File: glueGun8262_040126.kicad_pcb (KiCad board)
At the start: 2 copper layers, 121.9 x 76.8 mm, 62 parts, among them CN1 KF243-5.0-2P, CN2 KF243-5.0-2P, CN3 KF243-5.0-2P, CN4 KF243-5.0-2P, CN5 KF243-5.0-2P, CN6 KF243-5.0-2P, CN7 KF243-5.0-2P, CN9 KF243-5.0-4P, U1 DRV8262DDWR, U10 INA240A2DR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

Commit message: no drcErrors2 before replacing U5 to smt
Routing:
- net +48V: track 298.8 -> 284.9 mm
- net Net-(CN9-Pad4): track 11.4 -> 13.9 mm
- net Net-(U11-IN-): track 22.0 -> 19.7 mm
- net Net-(D4-K): track 7.27 -> 8.82 mm
- net /U1_OUT2: track 28.8 -> 29.5 mm
- net /U1_OUT3: track 14.9 -> 15.7 mm
- net Net-(D5-K): track 9.85 -> 10.6 mm
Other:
- board size 121.9 x 76.8 mm -> 121.9 x 78.1 mm

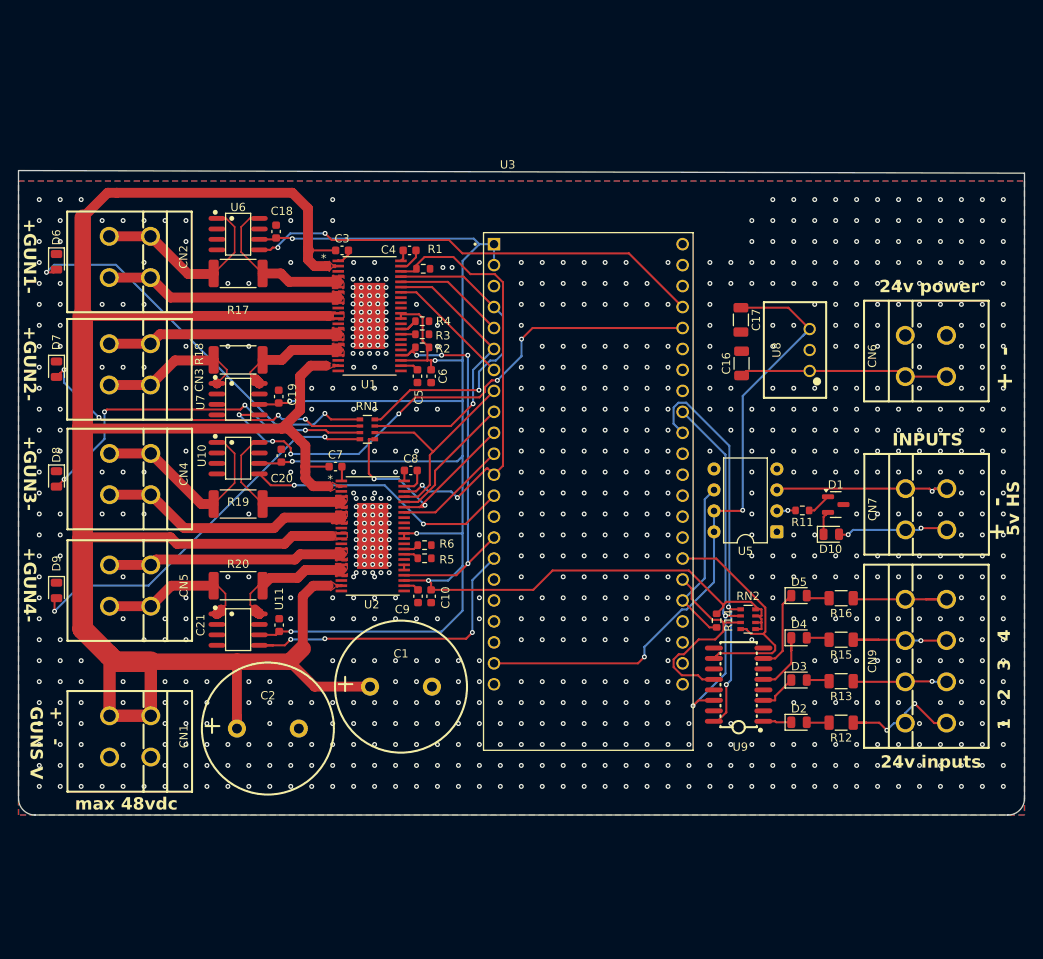
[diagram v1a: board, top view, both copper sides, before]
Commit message: added mounting holes
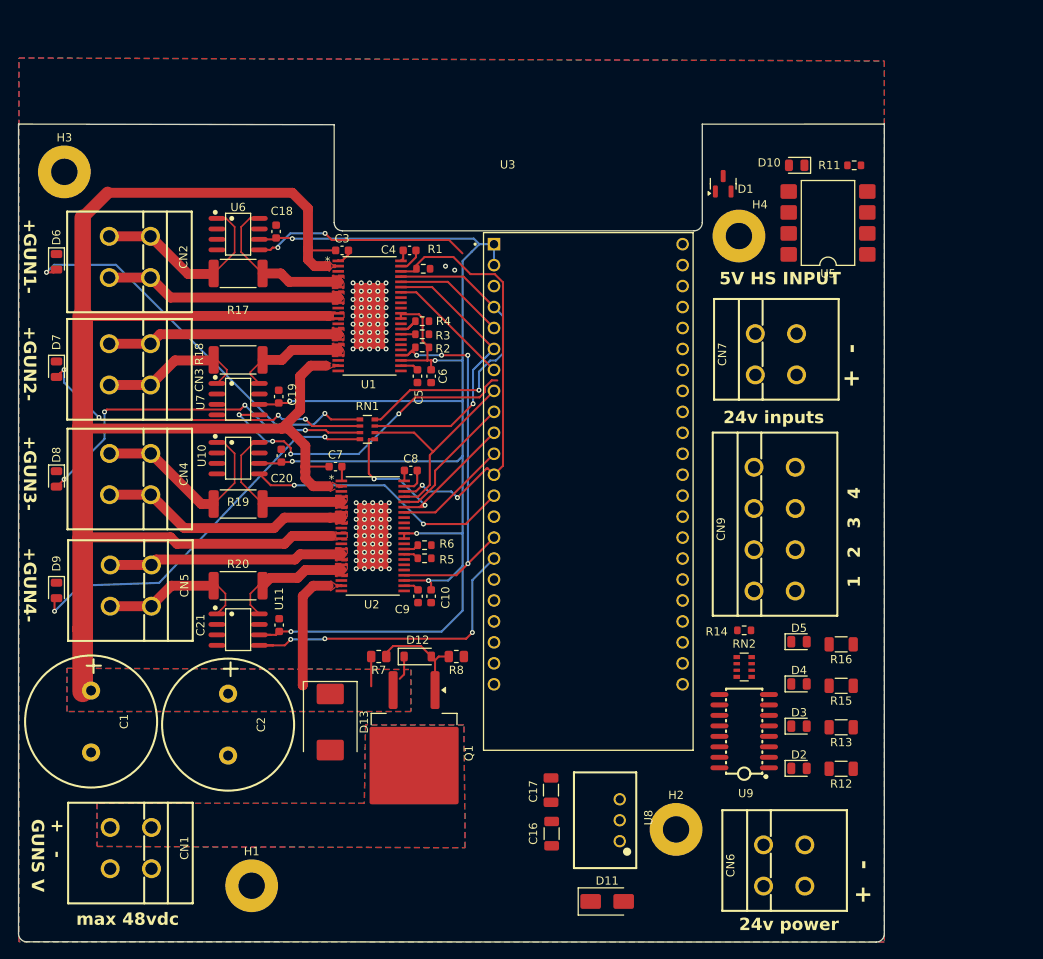
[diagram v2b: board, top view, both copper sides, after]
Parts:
- added D11: D, Diode_SMD:D_SMA, F.Cu at (177.5, 138.1)
- added D12: BZT52C15 zener, Diode_SMD:D_SOD-123, F.Cu at (154.6, 108.4)
- added D13: SMCJ51A, Diode_SMD:D_SMC, F.Cu at (144.0, 116.4)
- added H1: MountingHole_Pad, MountingHole:MountingHole_3.2mm_M3_Pad, F.Cu at (134.5, 136.2)
- added H2: MountingHole_Pad, MountingHole:MountingHole_3.2mm_M3_Pad, F.Cu at (185.9, 129.4)
- added H3: MountingHole_Pad, MountingHole:MountingHole_3.2mm_M3_Pad, F.Cu at (111.8, 49.7)
- added H4: MountingHole_Pad, MountingHole:MountingHole_3.2mm_M3_Pad, F.Cu at (193.5, 57.5)
- added Q1: SQM120P10-10m1L, Package_TO_SOT_SMD:TO-263-2, F.Cu at (154.1, 120.1)
- added R7: 100k, Resistor_SMD:R_0805_2012Metric, F.Cu at (149.9, 108.4)
- added R8: 47k, Resistor_SMD:R_0805_2012Metric, F.Cu at (159.3, 108.4)
- C17: value 22uf 10v -> 22uf 16v
- D1: value D_Schottky -> D_Schottky_AKK
- U5: footprint Package_DIP:DIP-8_W7.62mm -> Package_DIP:SMDIP-8_W9.53mm
- moved CN6 64.1 mm to (199.0, 133.8)
- moved U8 61.5 mm to (179.1, 128.3)
- moved C16 61.5 mm to (170.8, 129.9)
- moved C17 61.5 mm to (170.7, 124.6)
- moved D10 44.9 mm to (200.5, 48.9), turned to 180 degrees
- moved R11 42.3 mm to (207.5, 48.9), turned to 0 degrees
- moved D1 41.2 mm to (191.6, 51.1), turned to 90 degrees
- moved U5 37.9 mm to (204.3, 55.9)
- moved C1 37.8 mm to (115.0, 116.3), turned to -90 degrees
- moved CN7 26.2 mm to (198.0, 71.8)
- moved CN9 24.3 mm to (197.8, 93.0)
- moved CN1 13.5 mm to (119.8, 131.6)
- moved RN2 5.81 mm to (194.2, 109.7)
- moved U9 5.67 mm to (194.2, 117.5)
- moved D2 5.59 mm to (200.8, 122.0)
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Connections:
- C16 pad 1: Net-(U8-VIN) -> Net-(D11-K)
- CN1 pad 1: +48V -> Net-(Q1-D)
- CN6 pad 1: Net-(U8-VIN) -> Net-(D11-A)
- D1 pad 1: Net-(D1-K) -> Net-(D1-A)
- D1 pad 2: Net-(D1-A) -> unconnected-(D1-K-Pad2)
- D1 pad 3: (no net) -> Net-(D1-K-Pad3)
- R11 pad 1: Net-(D1-K) -> Net-(D1-K-Pad3)
- U8 pad 1: Net-(U8-VIN) -> Net-(D11-K)
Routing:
- net +5V: track 79.5 -> 0.00 mm, vias 2 -> 0
- net +48V: track 284.9 -> 230.4 mm
- net /Input_1_24v: track 48.9 -> 0.00 mm, vias 2 -> 0
- net +3V3: track 237.1 -> 188.7 mm
- net /Input_2_24v: track 44.3 -> 0.00 mm, vias 2 -> 0
- net /Input_4_24v: track 29.6 -> 0.00 mm
- net /Gun1Vref: track 56.0 -> 26.6 mm
- net /Gun2Vref: track 66.5 -> 40.2 mm, vias 6 -> 4
- net Net-(U8-VIN): track 25.4 -> 0.00 mm
- net /Input_3_24v: track 24.9 -> 0.00 mm
- net Net-(U5-C): track 22.8 -> 0.00 mm, vias 1 -> 0
- net /Input_0_5v: track 20.6 -> 0.00 mm
- net Net-(CN9-Pad1): track 16.4 -> 0.00 mm, vias 2 -> 0
- net Net-(CN9-Pad3): track 15.6 -> 0.00 mm, vias 1 -> 0
- net Net-(CN9-Pad4): track 13.9 -> 0.00 mm
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- added copper zone on B.Cu, net +48V
- added copper zone on B.Cu, net Net-(Q1-D)
- added copper zone on F.Cu, net Net-(Q1-D)
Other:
- board size 121.9 x 78.1 mm -> 104.9 x 99.1 mm
- board text added: "5V HS INPUT"
- board text removed: "5v HS"
- board text removed: "INPUTS"

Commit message: no drc errors with mounting holes
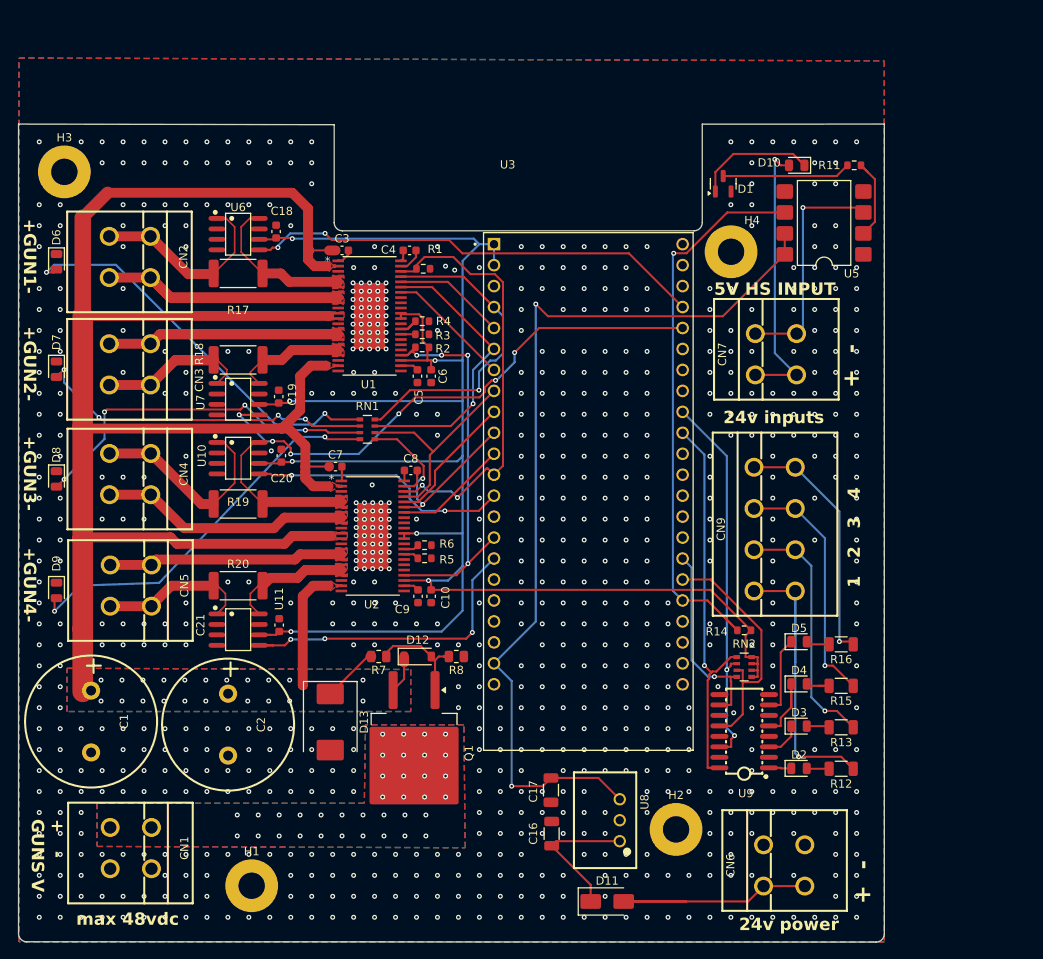
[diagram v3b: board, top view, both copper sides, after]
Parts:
- moved H4 2.13 mm to (192.6, 59.4)
- moved U5 0.48 mm to (203.8, 55.9)
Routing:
- net +5V: track 0.00 -> 112.4 mm, vias 0 -> 2
- net /Input_0_5v: track 0.00 -> 68.8 mm, vias 0 -> 1
- net +3V3: track 188.7 -> 239.0 mm
- net /Input_1_24v: track 0.00 -> 47.5 mm, vias 0 -> 1
- net /Input_2_24v: track 0.00 -> 46.5 mm, vias 0 -> 2
- net Net-(CN9-Pad1): track 0.00 -> 44.6 mm, vias 0 -> 1
- net Net-(D10-A): track 0.00 -> 34.2 mm, vias 0 -> 1
- net Net-(CN9-Pad2): track 0.00 -> 30.3 mm, vias 0 -> 1
- net Net-(D11-A): track 0.00 -> 30.3 mm
- net /Input_3_24v: track 0.00 -> 30.2 mm
- net Net-(CN9-Pad4): track 0.00 -> 30.2 mm, vias 0 -> 1
- net Net-(CN9-Pad3): track 0.00 -> 30.0 mm, vias 0 -> 1
- net /Gun1Vref: track 26.6 -> 56.0 mm
- net Net-(U5-C): track 0.00 -> 28.7 mm, vias 0 -> 1
- net /Gun2Vref: track 40.2 -> 66.2 mm, vias 4 -> 6
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
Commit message: add protection schotoky diode to 5v supply
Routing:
- net Net-(Q1-D): vias 36 -> 46
- net +48V: vias 21 -> 24
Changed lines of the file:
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@@
 	)
 	(via
+		(at 150.1775 113.82375)
+		(size 0.6)
+		(drill 0.3)
+		(layers "F.Cu" "B.Cu")
+		(free yes)
+		(net 2)
+	)
+	(via
 		(at 139.065 111.28375)
 		(size 0.6)
@@
 	)
 	(via
+		(at 143.8275 110.96625)
+		(size 0.6)
+		(drill 0.3)
+		(layers "F.Cu" "B.Cu")
+		(free yes)
+		(net 2)
+	)
+	(via
 		(at 118.745 111.28375)
 		(size 0.6)
@@
 	)
 	(via
+		(at 150.1775 111.28375)
+		(size 0.6)
+		(drill 0.3)
+		(layers "F.Cu" "B.Cu")
+		(free yes)
+		(net 2)
+	)
+	(via
 		(at 121.285 111.28375)
 		(size 0.6)
@@
 	)
 	(via
+		(at 125.095 130.175)
+		(size 0.6)
+		(drill 0.3)
+		(layers "F.Cu" "B.Cu")
+		(free yes)
+		(net 105)
+	)
+	(via
+		(at 157.95625 127.635)
+		(size 0.6)
+		(drill 0.3)
+		(layers "F.Cu" "B.Cu")
+		(free yes)
+		(net 105)
+	)
+	(via
+		(at 130.175 127.635)
+		(size 0.6)
+		(drill 0.3)
+		(layers "F.Cu" "B.Cu")
+		(free yes)
+		(net 105)
+	)
+	(via
+		(at 119.85625 127.635)
+		(size 0.6)
+		(drill 0.3)
+		(layers "F.Cu" "B.Cu")
+		(free yes)
+		(net 105)
+	)
+	(via
+		(at 132.715 127.635)
+		(size 0.6)
+		(drill 0.3)
+		(layers "F.Cu" "B.Cu")
+		(free yes)
+		(net 105)
+	)
+	(via
 		(at 140.335 130.175)
 		(size 0.6)
@@
 	)
 	(via
+		(at 157.95625 130.175)
+		(size 0.6)
+		(drill 0.3)
+		(layers "F.Cu" "B.Cu")
+		(free yes)
+		(net 105)
+	)
+	(via
 		(at 152.8763 117.8337)
 		(size 0.6)
@@
 	)
 	(via
+		(at 125.095 127.635)
+		(size 0.6)
+		(drill 0.3)
+		(layers "F.Cu" "B.Cu")
+		(free yes)
+		(net 105)
+	)
+	(via
 		(at 145.415 127.635)
 		(size 0.6)
@@
 	)
 	(via
-		(at 132.715 127.635)
+		(at 130.175 130.175)
 		(size 0.6)
 		(drill 0.3)
@@
 	)
 	(via
+		(at 127.635 127.635)
+		(size 0.6)
+		(drill 0.3)
+		(layers "F.Cu" "B.Cu")
+		(free yes)
+		(net 105)
+	)
+	(via
+		(at 127.635 130.175)
+		(size 0.6)
+		(drill 0.3)
+		(layers "F.Cu" "B.Cu")
+		(free yes)
+		(net 105)
+	)
+	(via
 		(at 147.955 130.175)
 		(size 0.6)
@@
 	)
 	(via
+		(at 119.85625 130.175)
+		(size 0.6)
+		(drill 0.3)
+		(layers "F.Cu" "B.Cu")
+		(free yes)
+		(net 105)
+	)
+	(via
 		(at 142.875 127.635)
 		(size 0.6)
@@
 		(polygon
 			(pts
-				(xy 106.25 35.891056) (xy 211.1375 36.238556) (xy 211.1375 143.03375) (xy 106.25 143)
+				(xy 106.25 43.60616) (xy 211.1375 43.95366) (xy 211.1375 143.03375) (xy 106.25 143)
 			)
 		)

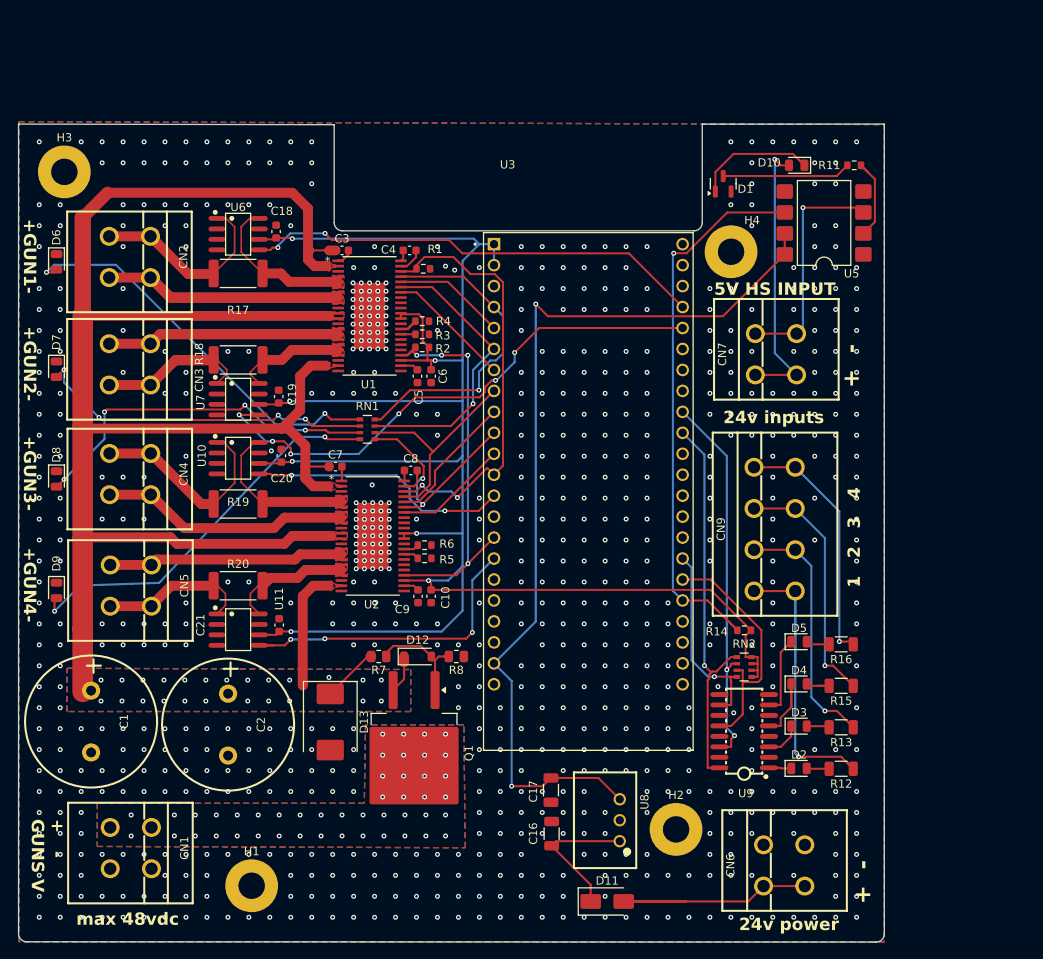
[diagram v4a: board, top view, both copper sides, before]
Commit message: pcb rewired new pinout
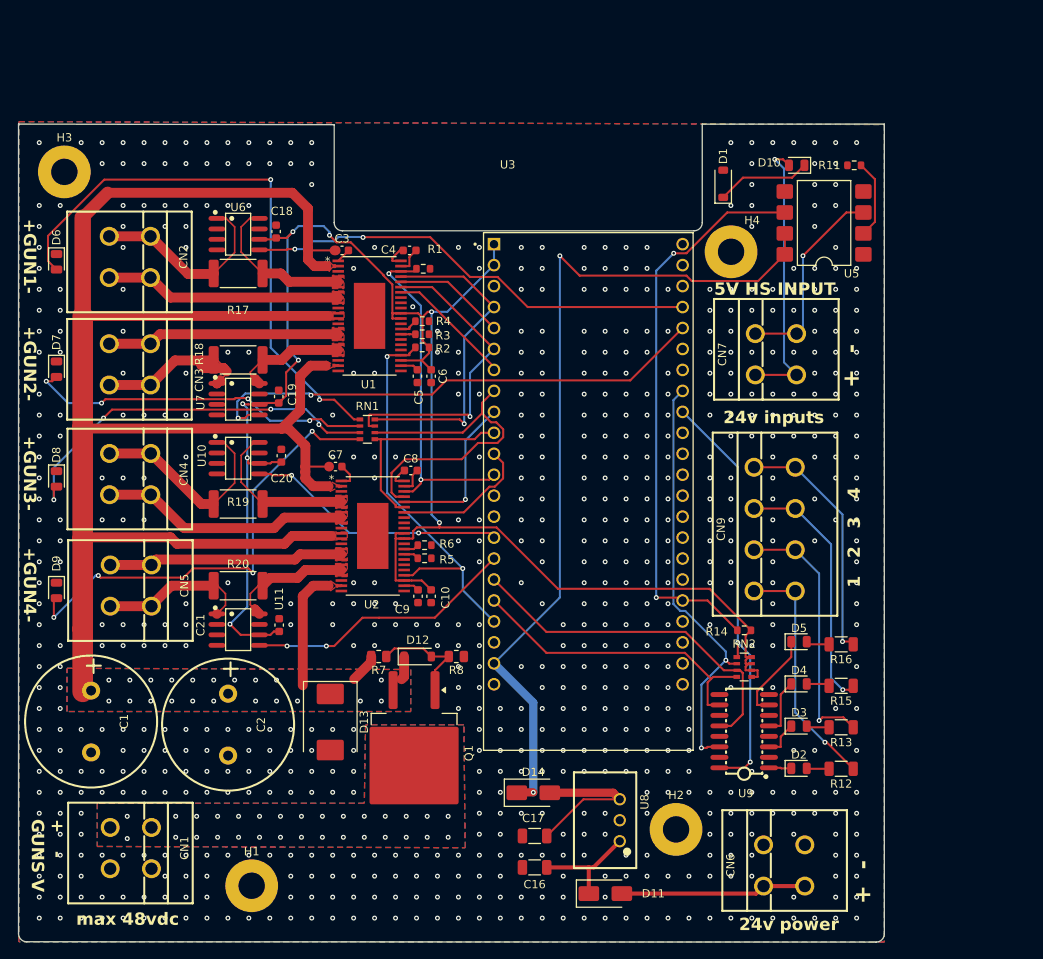
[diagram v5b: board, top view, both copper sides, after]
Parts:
- added D14: D_Schottky, Diode_SMD:D_SMA, F.Cu at (168.6, 124.9)
- D1: footprint Package_TO_SOT_SMD:SOT-23 -> Diode_SMD:D_SOD-123
- R11: value 150r -> 330r
- R14: value 5.1k -> 1k
- U3: value ESP32-S3-DEVKITC-1-N8R2 -> ESP32-S3-DEVKITC-1-N8R8
- moved C17 5.90 mm to (168.8, 130.2), turned to 180 degrees
- moved C16 4.58 mm to (168.8, 134.0), turned to 180 degrees
- moved D11 0.98 mm to (177.3, 137.2)
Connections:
- C17 pad 1: +5V -> Net-(D14-A)
- U3 pad J1_13: /Gun3Vref -> unconnected-(U3-GPIO3-PadJ1_13)
- U3 pad J1_15: /nFAULT -> /Gun3Vref
- U3 pad J1_17: unconnected-(U3-GPIO11-PadJ1_17) -> /Input_3_24v
- U3 pad J1_18: unconnected-(U3-GPIO12-PadJ1_18) -> /Input_4_24v
- U3 pad J1_19: unconnected-(U3-GPIO13-PadJ1_19) -> /nFAULT
- U3 pad J3_10: /Input_1_24v -> unconnected-(U3-GPIO38-PadJ3_10)
- U3 pad J3_16: /Input_4_24v -> unconnected-(U3-GPIO48-PadJ3_16)
- U3 pad J3_17: /Input_3_24v -> unconnected-(U3-GPIO47-PadJ3_17)
- U3 pad J3_8: unconnected-(U3-MTDO/GPIO40-PadJ3_8) -> /Input_2_24v
- U3 pad J3_9: /Input_2_24v -> /Input_1_24v
- U8 pad 3: +5V -> Net-(D14-A)
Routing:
- net /U1_OUT2: track 53.3 -> 29.5 mm
- net +3V3: track 239.0 -> 216.9 mm, vias 7 -> 8
- net /U1_OUT4: track 49.8 -> 28.2 mm
- net Net-(D6-A): track 48.8 -> 69.3 mm
- net Net-(D14-A): track 0.00 -> 19.5 mm
- net Net-(D1-K-Pad3): track 15.6 -> 0.00 mm
- net Net-(CN9-Pad1): track 44.6 -> 29.6 mm
- net /U2_IN1: track 26.4 -> 41.1 mm
- net /Input_4_24v: track 23.9 -> 38.2 mm, vias 1 -> 0
- net /Input_3_24v: track 30.2 -> 43.3 mm
- net /nSLEEP: track 52.0 -> 42.2 mm
- net Net-(D9-A): track 47.9 -> 55.8 mm, vias 2 -> 4
- net Net-(D11-A): track 30.3 -> 22.6 mm
- net +5V: track 112.4 -> 104.7 mm
- net +48V: track 237.1 -> 230.6 mm, vias 24 -> 21
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
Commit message: no drc errors
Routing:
- net Net-(U7-IN-): track 22.6 -> 18.1 mm
- net /U1_OUT3: track 14.4 -> 13.6 mm
- net /U2_OUT3: track 15.9 -> 15.1 mm
- net GND: vias 702 -> 718

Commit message: redesigned before freerouting
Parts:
- D1: value D_Schottky_AKK -> reverse protection; footprint Diode_SMD:D_SOD-123 -> Diode_SMD:D_SMA
- moved C1 76.6 mm to (151.3, 48.8)
- moved R8 24.6 mm to (141.5, 125.5), turned to 0 degrees
- moved C2 22.9 mm to (154.0, 111.9), turned to 0 degrees
- moved R12 21.5 mm to (205.1, 100.5), turned to -90 degrees
- moved Q1 19.2 mm to (135.0, 118.5), turned to 180 degrees
- moved D2 17.6 mm to (205.4, 104.9), turned to 90 degrees
- moved R13 17.5 mm to (200.0, 100.5), turned to -90 degrees
- moved R7 17.0 mm to (146.5, 125.1), turned to 90 degrees
- moved U3 16.9 mm to (174.5, 71.5)
- moved D12 16.9 mm to (149.5, 124.5), turned to -90 degrees
- moved C16 16.8 mm to (167.5, 117.2)
- moved C17 16.8 mm to (167.5, 113.4)
- moved U8 16.8 mm to (177.8, 111.5)
- moved D11 16.8 mm to (176.0, 120.4)
- moved D14 16.8 mm to (167.3, 108.2)
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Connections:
- D1 pad 1: Net-(D1-A) -> Net-(D1-K)
- D1 pad 2: unconnected-(D1-K-Pad2) -> Net-(D1-A)
- R11 pad 1: Net-(D1-K-Pad3) -> Net-(D1-K)
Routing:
- net +3V3: track 216.9 -> 0.00 mm, vias 8 -> 0
- net +5V: track 104.7 -> 0.00 mm, vias 2 -> 0
- net /Input_0_5v: track 69.6 -> 0.00 mm, vias 2 -> 0
- net Net-(D6-A): track 69.3 -> 0.00 mm, vias 2 -> 0
- net /Gun2Vref: track 62.6 -> 0.00 mm, vias 2 -> 0
- net Net-(D9-A): track 55.8 -> 0.00 mm, vias 4 -> 0
- net /Gun1Vref: track 55.5 -> 0.00 mm, vias 2 -> 0
- net /Input_2_24v: track 51.7 -> 0.00 mm, vias 2 -> 0
- net /Input_1_24v: track 51.7 -> 0.00 mm, vias 2 -> 0
- net /nFAULT: track 48.9 -> 0.00 mm, vias 2 -> 0
- net Net-(D8-A): track 47.0 -> 0.00 mm, vias 4 -> 0
- net /Input_3_24v: track 43.3 -> 0.00 mm
- net Net-(D7-A): track 42.4 -> 0.00 mm, vias 4 -> 0
- net /nSLEEP: track 42.2 -> 0.00 mm, vias 2 -> 0
- net /U2_IN1: track 41.1 -> 0.00 mm
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- removed copper zone on B.Cu, net Net-(Q1-D)
- removed copper zone on F.Cu, net Net-(Q1-D)
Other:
- board size 104.9 x 99.1 mm -> 104 x 93 mm

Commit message: minor mounting hole position mostly git test
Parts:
- moved H3 4.69 mm to (112.0, 45.0)
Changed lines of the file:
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@@
 	(footprint "MountingHole:MountingHole_3.2mm_M3_Pad"
 		(layer "F.Cu")
-		(at 111.76 49.6887)
+		(at 112 45)
 		(descr "Mounting Hole 3.2mm, M3, generated by kicad-footprint-generator mountinghole.py")
 		(tags "mountinghole M3")
